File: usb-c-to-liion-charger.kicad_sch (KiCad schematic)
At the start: 4 parts

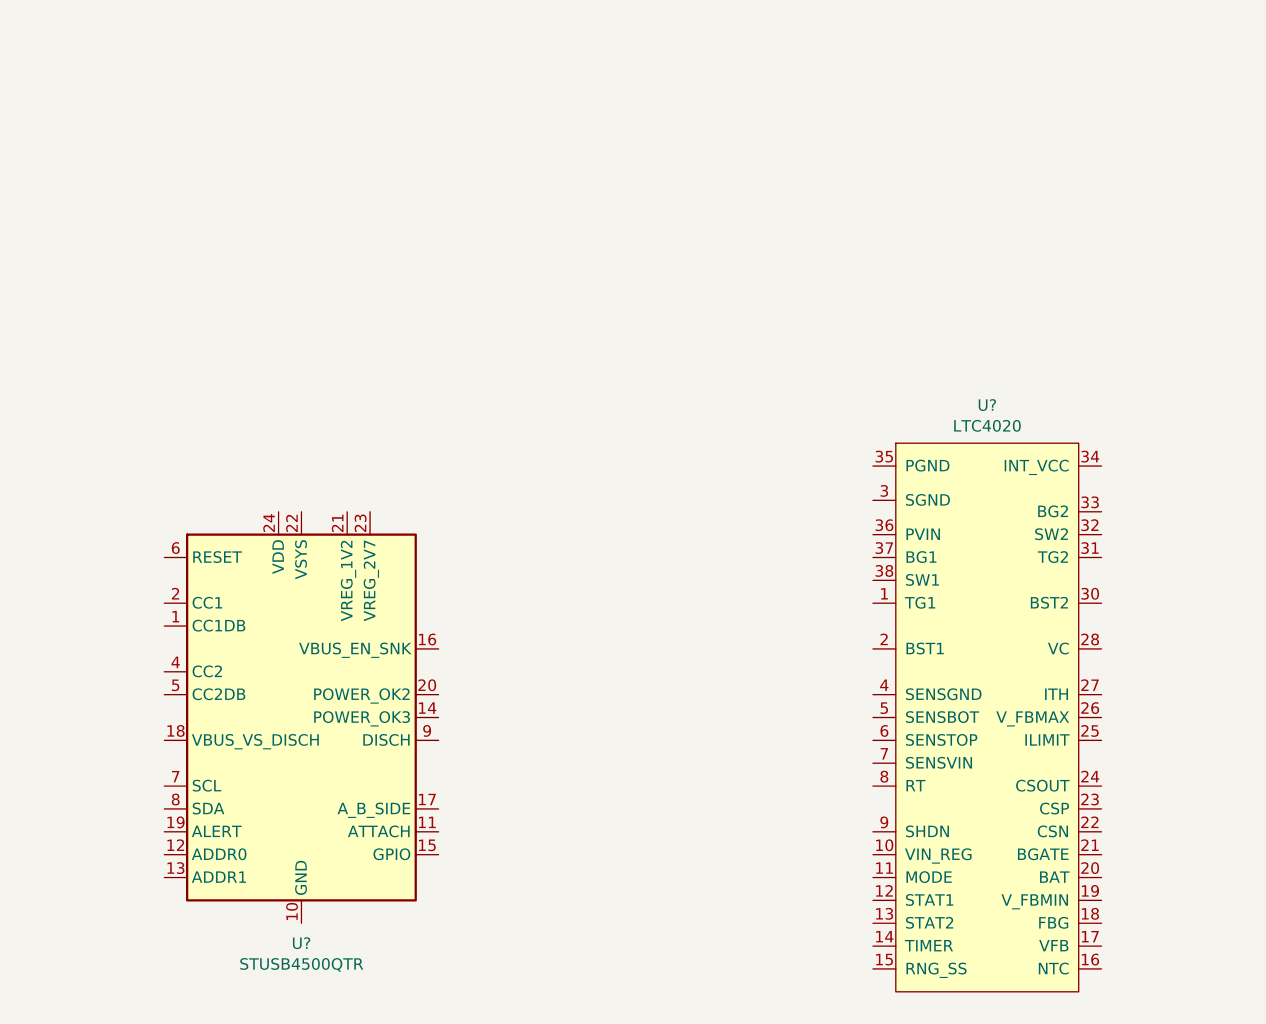
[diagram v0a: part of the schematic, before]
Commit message: Add LTC4000 and LTC3789
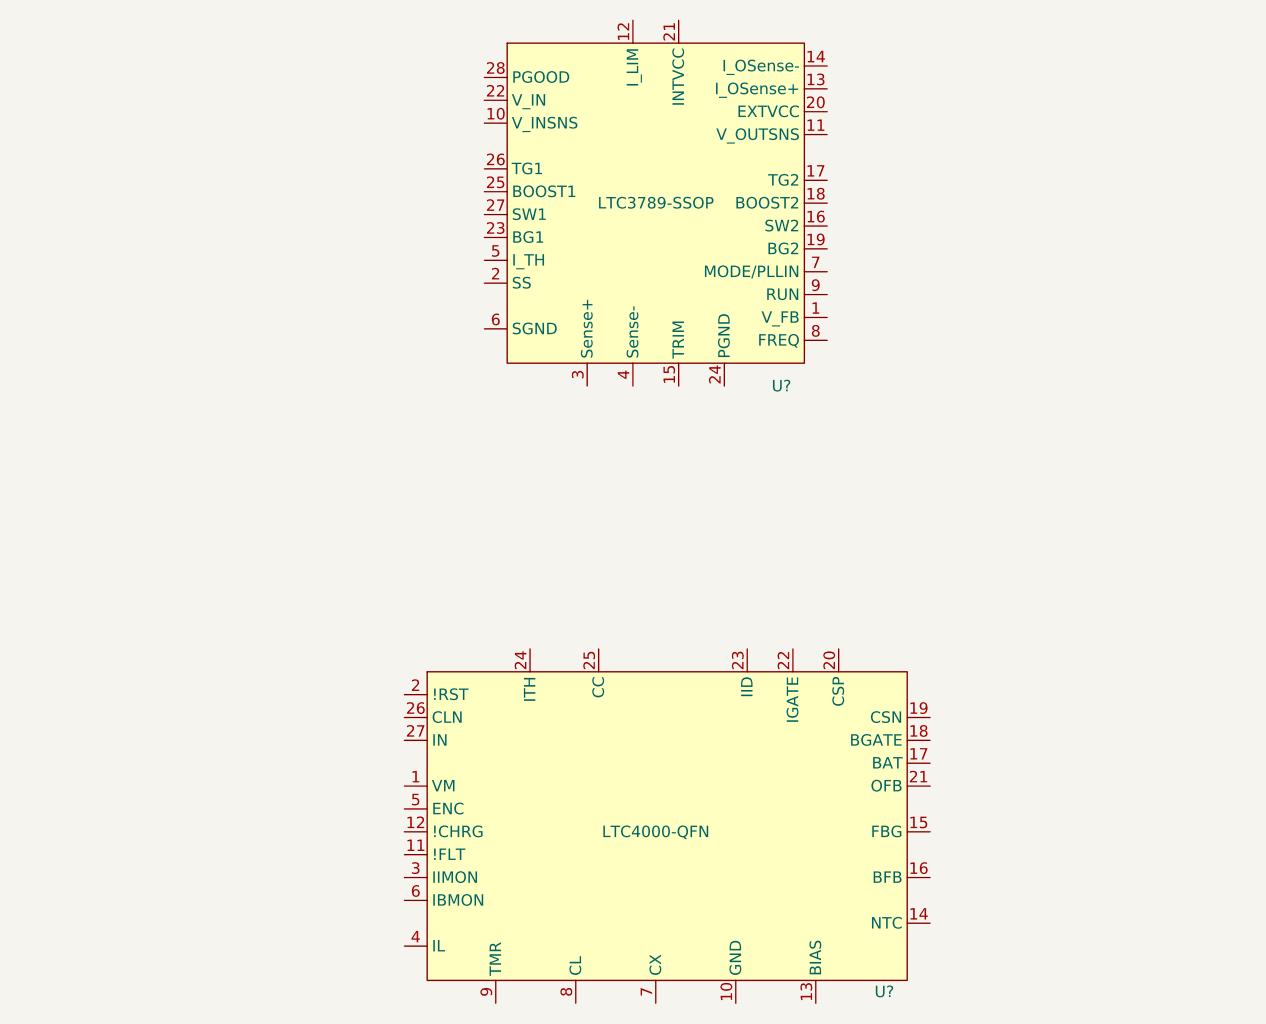
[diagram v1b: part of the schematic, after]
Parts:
- removed U?: STUSB4500QTR, Package_DFN_QFN:QFN-24-1EP_4x4mm_P0.5mm_EP2.7x2.7mm, symbol Interface_USB:STUSB4500QTR
- removed U?: LTC4020, Package_DFN_QFN:QFN-38-1EP_5x7mm_P0.5mm_EP3.15x5.15mm_ThermalVias, symbol extraSymbols:LTC4020
- added U?: LTC4000-QFN, Package_DFN_QFN:QFN-28-1EP_4x5mm_P0.5mm_EP2.65x3.65mm_ThermalVias, symbol extraSymbols:LTC4000-QFN
- added U?: LTC3789-SSOP, Package_SO:SSOP-28_3.9x9.9mm_P0.635mm, symbol extraSymbols:LTC3789-SSOP
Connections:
- new net: U?.10 (GND), U?.28 (GND), U?.29 (GND)
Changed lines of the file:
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@@
 (kicad_sch (version 20211123) (generator eeschema)
   (paper "A4")
-  (symbol (lib_id "Interface_USB:STUSB4500QTR") (at 100.33 102.87 0) (unit 1)
-    (in_bom yes) (on_board yes)
-    (property "Reference" "U?" (id 0) (at 100.33 127.9906 0))
-    (property "Value" "STUSB4500QTR" (id 1) (at 100.33 130.302 0))
-    (property "Footprint" "Package_DFN_QFN:QFN-24-1EP_4x4mm_P0.5mm_EP2.7x2.7mm" (id 2) (at 100.33 102.87 0)
-      (effects (font (size 1.27 1.27)) hide)
-    )
-    (property "Datasheet" "https://www.st.com/resource/en/datasheet/stusb4500.pdf" (id 3) (at 100.33 102.87 0)
-      (effects (font (size 1.27 1.27)) hide)
-    )
-    (pin "1")
-    (pin "10")
-    (pin "11")
-    (pin "12")
-    (pin "13")
-    (pin "14")
-    (pin "15")
-    (pin "16")
-    (pin "17")
-    (pin "18")
-    (pin "19")
-    (pin "2")
-    (pin "20")
-    (pin "21")
-    (pin "22")
-    (pin "23")
-    (pin "24")
-    (pin "25")
-    (pin "3")
-    (pin "4")
-    (pin "5")
-    (pin "6")
-    (pin "7")
-    (pin "8")
-    (pin "9")
-  )
   (symbol (lib_id "Connector:USB_C_Receptacle_USB2.0") (at 33.02 104.14 0) (unit 1)
     (in_bom yes) (on_board yes)
@@
     (pin "S1")
   )
-  (symbol (lib_id "extraSymbols:LTC4020") (at 176.53 120.65 0) (unit 1)
+  (symbol (lib_id "Device:Battery") (at 226.06 104.14 0) (unit 1)
     (in_bom yes) (on_board yes)
-    (property "Reference" "U?" (id 0) (at 176.53 68.199 0))
-    (property "Value" "LTC4020" (id 1) (at 176.53 70.5104 0))
-    (property "Footprint" "Package_DFN_QFN:QFN-38-1EP_5x7mm_P0.5mm_EP3.15x5.15mm_ThermalVias" (id 2) (at 176.53 121.92 0)
+    (property "Reference" "BT?" (id 0) (at 228.8032 102.9716 0)
+      (effects (font (size 1.27 1.27)) (justify left))
+    )
+    (property "Value" "Battery" (id 1) (at 228.8032 105.283 0)
+      (effects (font (size 1.27 1.27)) (justify left))
+    )
+    (property "Footprint" "" (id 2) (at 226.06 102.616 90)
       (effects (font (size 1.27 1.27)) hide)
     )
-    (property "Datasheet" "https://www.analog.com/media/en/technical-documentation/data-sheets/4020fd.pdf" (id 3) (at 176.53 121.92 0)
+    (property "Datasheet" "~" (id 3) (at 226.06 102.616 90)
+      (effects (font (size 1.27 1.27)) hide)
+    )
+    (pin "1")
+    (pin "2")
+  )
+  (symbol (lib_id "extraSymbols:LTC4000-QFN") (at 139.7 115.57 0) (unit 1)
+    (in_bom yes) (on_board yes)
+    (property "Reference" "U?" (id 0) (at 165.1 133.35 0))
+    (property "Value" "LTC4000-QFN" (id 1) (at 139.7 115.57 0))
+    (property "Footprint" "Package_DFN_QFN:QFN-28-1EP_4x5mm_P0.5mm_EP2.65x3.65mm_ThermalVias" (id 2) (at 139.7 111.76 0)
+      (effects (font (size 1.27 1.27)) hide)
+    )
+    (property "Datasheet" "https://www.analog.com/media/en/technical-documentation/data-sheets/4000fb.pdf" (id 3) (at 139.7 111.76 0)
       (effects (font (size 1.27 1.27)) hide)
     )
@@
     (pin "29")
     (pin "3")
-    (pin "30")
-    (pin "31")
-    (pin "32")
-    (pin "33")
-    (pin "34")
-    (pin "35")
-    (pin "36")
-    (pin "37")
-    (pin "38")
-    (pin "39")
     (pin "4")
     (pin "5")
@@
     (pin "9")
   )
-  (symbol (lib_id "Device:Battery") (at 226.06 104.14 0) (unit 1)
-    (in_bom yes) (on_board yes)
-    (property "Reference" "BT?" (id 0) (at 228.8032 102.9716 0)
-      (effects (font (size 1.27 1.27)) (justify left))
-    )
-    (property "Value" "Battery" (id 1) (at 228.8032 105.283 0)
-      (effects (font (size 1.27 1.27)) (justify left))
-    )
-    (property "Footprint" "" (id 2) (at 226.06 102.616 90)
+  (symbol (lib_id "extraSymbols:LTC3789-SSOP") (at 139.7 45.72 0) (unit 1)
+    (in_bom yes) (on_board yes) (fields_autoplaced)
+    (property "Reference" "U?" (id 0) (at 153.67 66.04 0))
+    (property "Value" "LTC3789-SSOP" (id 1) (at 139.7 45.72 0))
+    (property "Footprint" "Package_SO:SSOP-28_3.9x9.9mm_P0.635mm" (id 2) (at 139.7 44.45 0)
       (effects (font (size 1.27 1.27)) hide)
     )
-    (property "Datasheet" "~" (id 3) (at 226.06 102.616 90)
+    (property "Datasheet" "https://www.analog.com/media/en/technical-documentation/data-sheets/3789fc.pdf" (id 3) (at 137.16 45.72 0)
       (effects (font (size 1.27 1.27)) hide)
     )
     (pin "1")
+    (pin "10")
+    (pin "11")
+    (pin "12")
+    (pin "13")
+    (pin "14")
+    (pin "15")
+    (pin "16")
+    (pin "17")
+    (pin "18")
+    (pin "19")
     (pin "2")
+    (pin "20")
+    (pin "21")
+    (pin "22")
+    (pin "23")
+    (pin "24")
+    (pin "25")
+    (pin "26")
+    (pin "27")
+    (pin "28")
+    (pin "3")
+    (pin "4")
+    (pin "5")
+    (pin "6")
+    (pin "7")
+    (pin "8")
+    (pin "9")
   )
   (sheet_instances
@@
       (reference "J?") (unit 1) (value "USB_C_Receptacle_USB2.0") (footprint "")
     )
-    (path "/00000000-0000-0000-0000-000061aba05d"
-      (reference "U?") (unit 1) (value "STUSB4500QTR") (footprint "Package_DFN_QFN:QFN-24-1EP_4x4mm_P0.5mm_EP2.7x2.7mm")
+    (path "/0f9e3193-8cb4-41fe-a291-a950c4ea027a"
+      (reference "U?") (unit 1) (value "LTC4000-QFN") (footprint "Package_DFN_QFN:QFN-28-1EP_4x5mm_P0.5mm_EP2.65x3.65mm_ThermalVias")
     )
-    (path "/00000000-0000-0000-0000-000061ac4aa4"
-      (reference "U?") (unit 1) (value "LTC4020") (footprint "Package_DFN_QFN:QFN-38-1EP_5x7mm_P0.5mm_EP3.15x5.15mm_ThermalVias")
+    (path "/184a8f36-c8af-41e0-b93a-6530fc2113a5"
+      (reference "U?") (unit 1) (value "LTC3789-SSOP") (footprint "Package_SO:SSOP-28_3.9x9.9mm_P0.635mm")
     )
   )

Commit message: WIP charge IC
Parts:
- removed U?: LTC4000-QFN, Package_DFN_QFN:QFN-28-1EP_4x5mm_P0.5mm_EP2.65x3.65mm_ThermalVias, symbol extraSymbols:LTC4000-QFN
- added C?: ~, symbol Device:C_Polarized
- added C? (x3): ~, symbol Device:C
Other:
- added sheet Charge-IC (Charge-IC.kicad_sch)

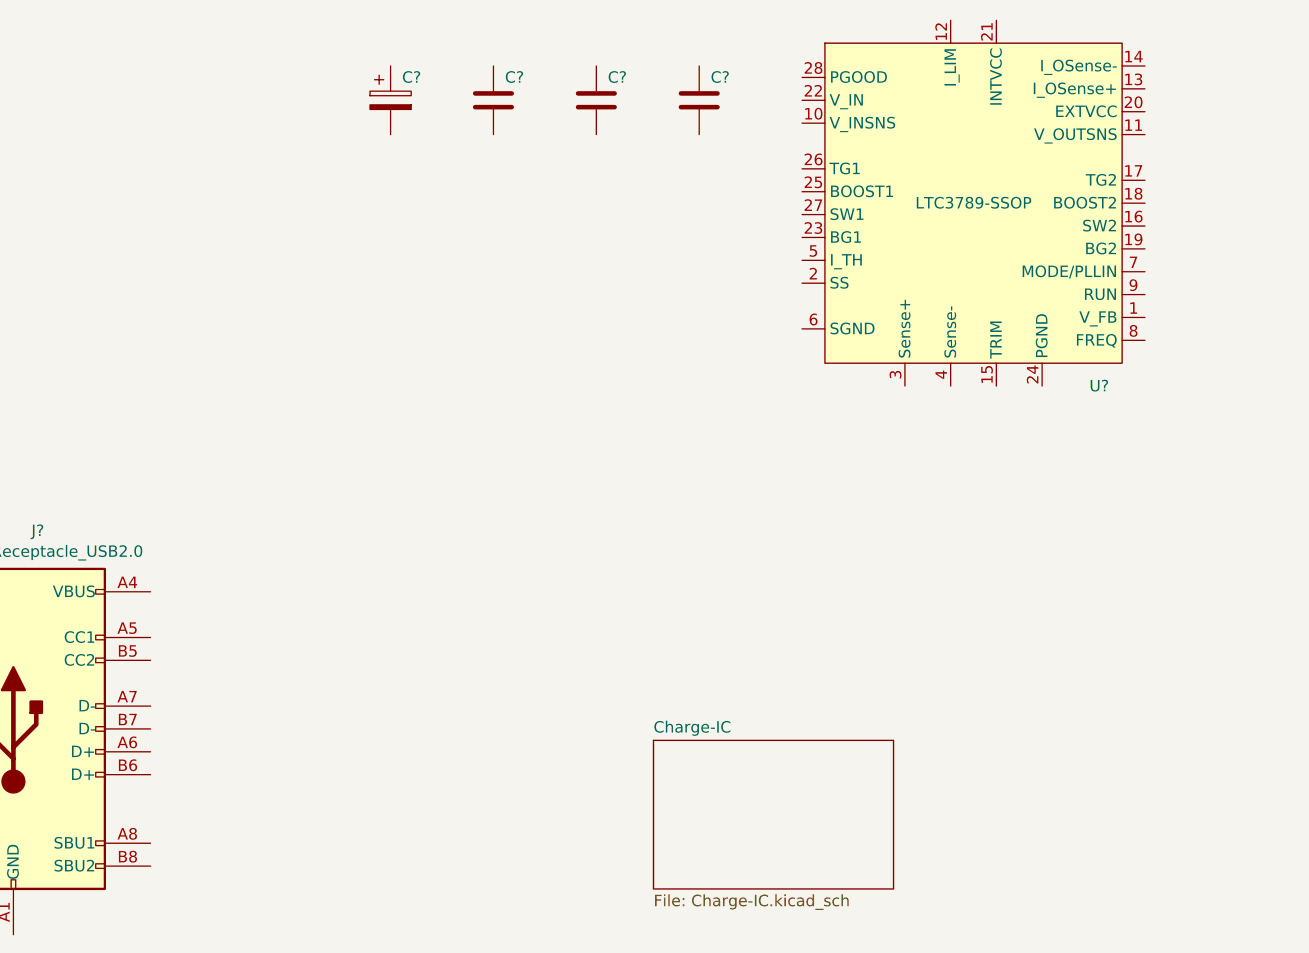
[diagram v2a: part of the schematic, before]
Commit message: Finish Charge IC, WIP boost converter, add LTC3769
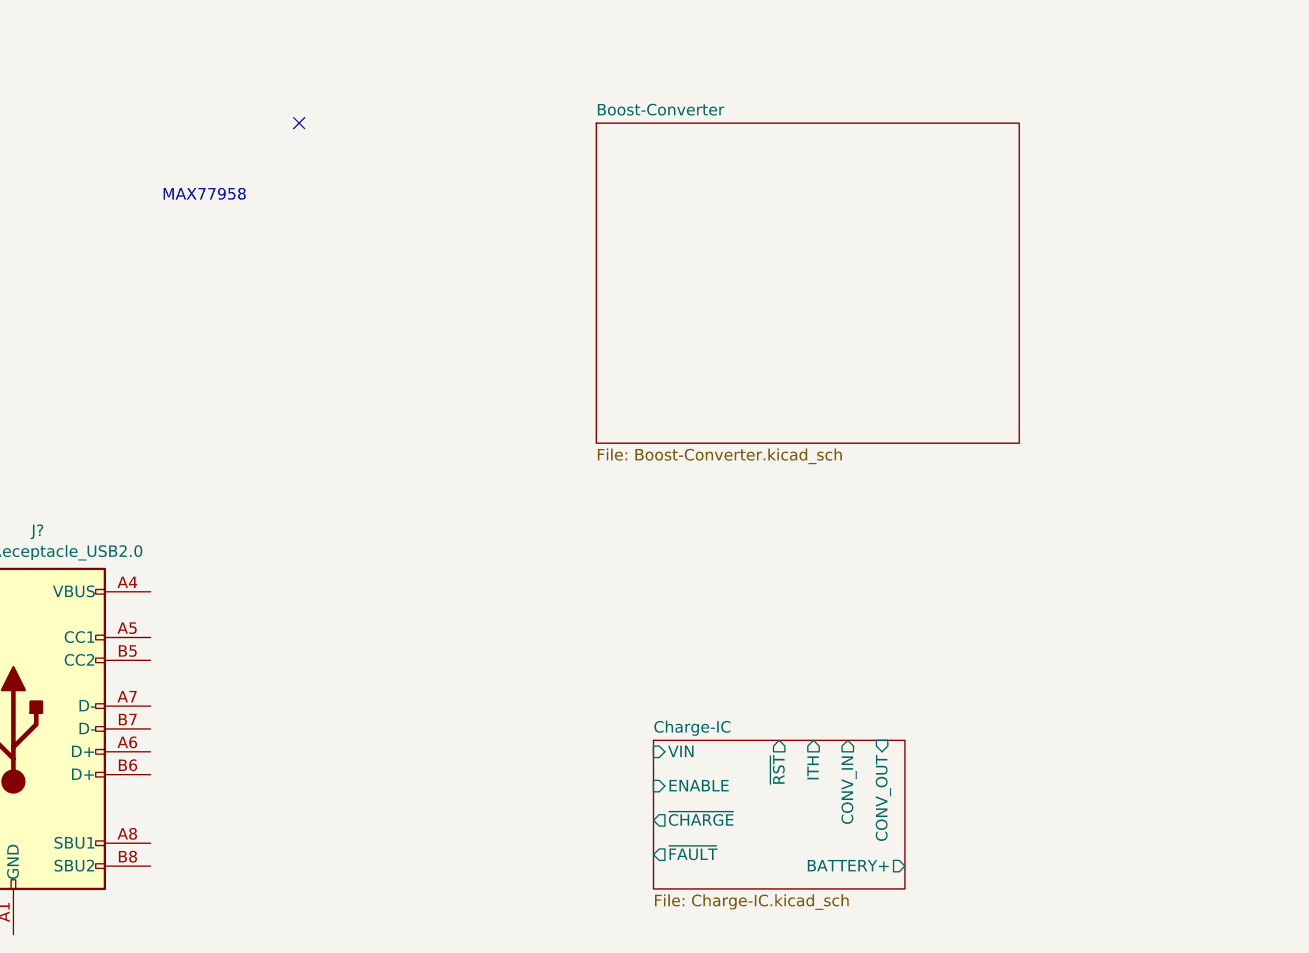
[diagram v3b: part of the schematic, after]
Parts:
- removed C?: ~, symbol Device:C_Polarized
- removed C? (x3): ~, symbol Device:C
- removed U?: LTC3789-SSOP, Package_SO:SSOP-28_3.9x9.9mm_P0.635mm, symbol extraSymbols:LTC3789-SSOP
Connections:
- no-connect marks 0 -> 1
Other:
- added sheet Boost-Converter (Boost-Converter.kicad_sch)
- sheet Charge-IC ports: added BATTERY+, CONV_IN, CONV_OUT, ENABLE, ITH, VIN, ~{CHARGE}, ~{FAULT}, ~{RST}; removed none
- note added: "MAX77958"

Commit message: Finish boost converter
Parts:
- added U?: (no value), symbol Interface_USB:STUSB4500QTR
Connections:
- new net: U?.10 (GND), U?.25 (GND)
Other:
- sheet Boost-Converter ports: added ITH, SS, V_{IN}, V_{OUT}; removed none
- note added: "If no voltage is given, then for all caps 6.3V are stated"
